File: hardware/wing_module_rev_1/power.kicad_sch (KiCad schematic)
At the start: 18 parts, among them U2 TPS563201, U3 BL9161G-33, U4 TPS7A8101

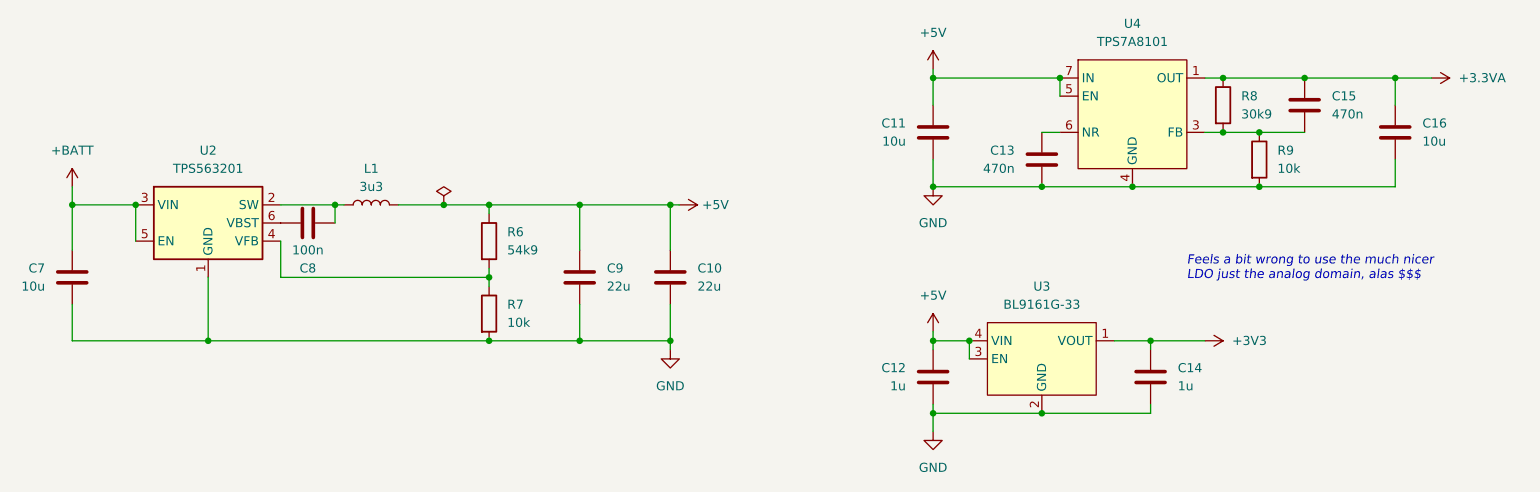
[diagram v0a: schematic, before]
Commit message: Reassigned reference numbers
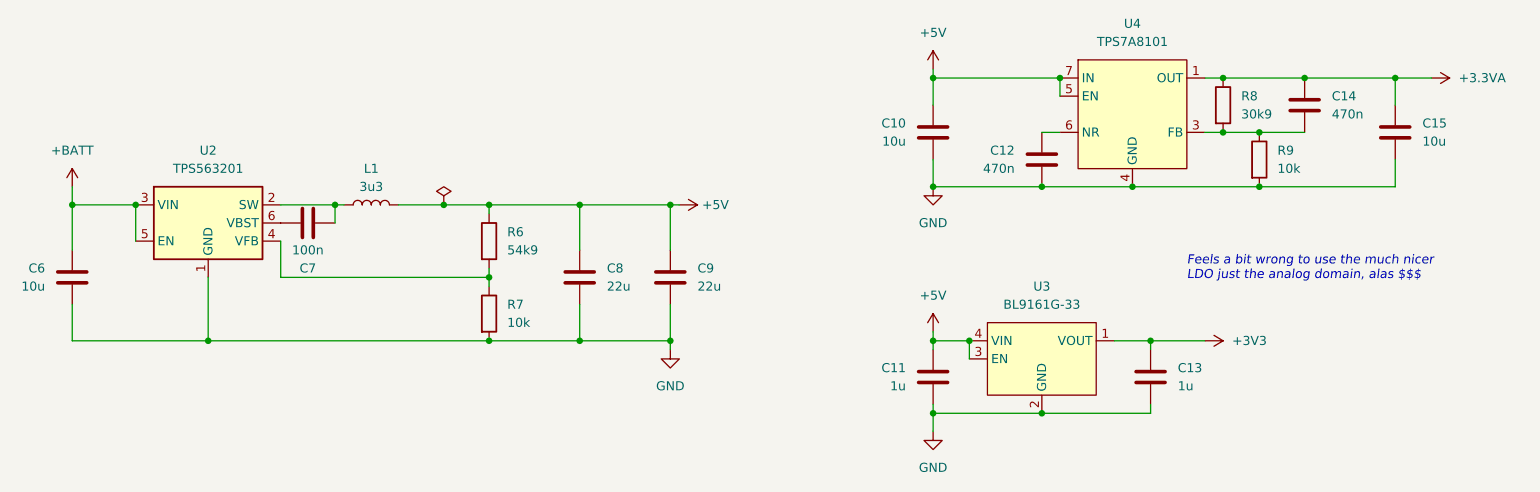
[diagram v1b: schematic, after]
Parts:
- renumbered C11 to C10, C12 to C11, C13 to C12, C14 to C13, C15 to C14, C16 to C15, C7 to C6, C8 to C7, C9 to C8, C10 to C9
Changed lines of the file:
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@@
 		(on_board yes)
 		(dnp no)
-		(property "Reference" "C12"
+		(property "Reference" "C11"
 			(at 167.64 110.4899 0)
 			(effects
@@
 			(project "wing_module_rev_1"
 				(path "/7b7fffa9-e888-4279-94bf-385d74cf78f9/0600a7c1-aaf8-4e35-a4dc-6a72af769bde"
-					(reference "C12")
+					(reference "C11")
 					(unit 1)
 				)
@@
 		(on_board yes)
 		(dnp no)
-		(property "Reference" "C14"
+		(property "Reference" "C13"
 			(at 205.74 110.4899 0)
 			(effects
@@
 			(project "wing_module_rev_1"
 				(path "/7b7fffa9-e888-4279-94bf-385d74cf78f9/0600a7c1-aaf8-4e35-a4dc-6a72af769bde"
-					(reference "C14")
+					(reference "C13")
 					(unit 1)
 				)
@@
 		(on_board yes)
 		(dnp no)
-		(property "Reference" "C8"
+		(property "Reference" "C7"
 			(at 83.82 96.52 90)
 			(effects
@@
 			(project "wing_module_rev_1"
 				(path "/7b7fffa9-e888-4279-94bf-385d74cf78f9/0600a7c1-aaf8-4e35-a4dc-6a72af769bde"
-					(reference "C8")
+					(reference "C7")
 					(unit 1)
 				)
@@
 		(dnp no)
 		(fields_autoplaced yes)
-		(property "Reference" "C15"
+		(property "Reference" "C14"
 			(at 227.33 72.3899 0)
 			(effects
@@
 			(project "wing_module_rev_1"
 				(path "/7b7fffa9-e888-4279-94bf-385d74cf78f9/0600a7c1-aaf8-4e35-a4dc-6a72af769bde"
-					(reference "C15")
+					(reference "C14")
 					(unit 1)
 				)
@@
 		(on_board yes)
 		(dnp no)
-		(property "Reference" "C13"
+		(property "Reference" "C12"
 			(at 182.88 80.01 0)
 			(effects
@@
 			(project "wing_module_rev_1"
 				(path "/7b7fffa9-e888-4279-94bf-385d74cf78f9/0600a7c1-aaf8-4e35-a4dc-6a72af769bde"
-					(reference "C13")
+					(reference "C12")
 					(unit 1)
 				)
@@
 		(on_board yes)
 		(dnp no)
-		(property "Reference" "C11"
+		(property "Reference" "C10"
 			(at 167.64 76.1999 0)
 			(effects
@@
 			(project "wing_module_rev_1"
 				(path "/7b7fffa9-e888-4279-94bf-385d74cf78f9/0600a7c1-aaf8-4e35-a4dc-6a72af769bde"
-					(reference "C11")
+					(reference "C10")
 					(unit 1)
 				)
@@
 		(on_board yes)
 		(dnp no)
-		(property "Reference" "C9"
+		(property "Reference" "C8"
 			(at 125.73 96.5199 0)
 			(effects
@@
 			(project "wing_module_rev_1"
 				(path "/7b7fffa9-e888-4279-94bf-385d74cf78f9/0600a7c1-aaf8-4e35-a4dc-6a72af769bde"
-					(reference "C9")
+					(reference "C8")
 					(unit 1)
 				)
@@
 		(on_board yes)
 		(dnp no)
-		(property "Reference" "C10"
+		(property "Reference" "C9"
 			(at 138.43 96.5199 0)
 			(effects
@@
 			(project "wing_module_rev_1"
 				(path "/7b7fffa9-e888-4279-94bf-385d74cf78f9/0600a7c1-aaf8-4e35-a4dc-6a72af769bde"
-					(reference "C10")
+					(reference "C9")
 					(unit 1)
 				)
@@
 		(on_board yes)
 		(dnp no)
-		(property "Reference" "C16"
+		(property "Reference" "C15"
 			(at 240.03 76.1999 0)
 			(effects
@@
 			(project "wing_module_rev_1"
 				(path "/7b7fffa9-e888-4279-94bf-385d74cf78f9/0600a7c1-aaf8-4e35-a4dc-6a72af769bde"
-					(reference "C16")
+					(reference "C15")
 					(unit 1)
 				)
@@
 		(on_board yes)
 		(dnp no)
-		(property "Reference" "C7"
+		(property "Reference" "C6"
 			(at 46.99 96.5199 0)
 			(effects
@@
 			(project "wing_module_rev_1"
 				(path "/7b7fffa9-e888-4279-94bf-385d74cf78f9/0600a7c1-aaf8-4e35-a4dc-6a72af769bde"
-					(reference "C7")
-					(unit 1)
-				)
+					(reference "C6")
+					(unit 1)
+				)
